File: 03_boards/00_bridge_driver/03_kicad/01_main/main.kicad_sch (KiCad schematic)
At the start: 0 parts

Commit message: Week 0x4 - Spatial ROMs are hard.... (#25)
* Reference document with bootstrap selection calculations

* Boot strap capacitors, resistors and diode work for triple half bridge driver

* Few small changes to reduced order model

* Reduced order model under FOC control

* Finished initial reduced order model

* Custom motor model that needs to be validated and graphs

* Rename to 00_reduced_order_model and Updated readme.md

* Few changes to the model model & Selected Boot Diodes

* Began work on the refactored reduced order model

* New parameter file, removed library and added derived equations

* Initial draft of reduced order model

* Moving pole equation around. Solver not working.

* Issues with the field modelling

* Few additional changes before merge
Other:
- added sheet Drivers (Drivers.kicad_sch)
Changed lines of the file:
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@@
+		)
+	)
+	(sheet
+		(at 238.76 144.78)
+		(size 26.67 3.81)
+		(exclude_from_sim no)
+		(in_bom yes)
+		(on_board yes)
+		(dnp no)
+		(fields_autoplaced yes)
+		(stroke
+			(width 0.1524)
+			(type solid)
+		)
+		(fill
+			(color 0 0 0 0)
+		)
+		(property "Sheetname" "Drivers"
+			(at 238.76 144.0684 0)
+			(show_name no)
+			(do_not_autoplace no)
+			(effects
+				(font
+					(size 1.27 1.27)
+				)
+				(justify left bottom)
+			)
+		)
+		(property "Sheetfile" "Drivers.kicad_sch"
+			(at 238.76 149.1746 0)
+			(show_name no)
+			(do_not_autoplace no)
+			(effects
+				(font
+					(size 1.27 1.27)
+				)
+				(justify left top)
+			)
+		)
+		(instances
+			(project "main"
+				(path "/221b5544-ca14-4503-b001-a85fc346b8a9"
+					(page "3")
+				)
+			)
 		)
 	)

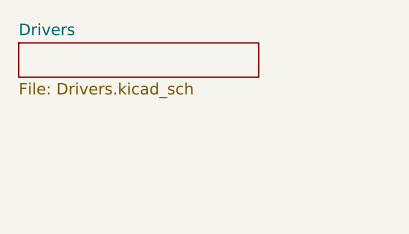
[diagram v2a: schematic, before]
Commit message: Triple bridge driver layout
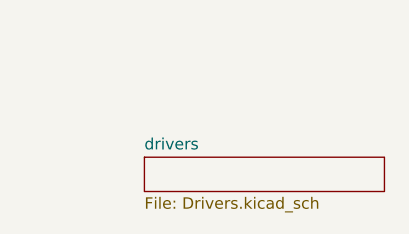
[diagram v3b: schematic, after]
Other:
- sheet Drivers renamed drivers
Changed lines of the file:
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@@
 	)
 	(sheet
-		(at 238.76 144.78)
+		(at 252.73 157.48)
 		(size 26.67 3.81)
 		(exclude_from_sim no)
@@
 			(color 0 0 0 0)
 		)
-		(property "Sheetname" "Drivers"
-			(at 238.76 144.0684 0)
+		(property "Sheetname" "drivers"
+			(at 252.73 156.7684 0)
 			(show_name no)
 			(do_not_autoplace no)
@@
 		)
 		(property "Sheetfile" "Drivers.kicad_sch"
-			(at 238.76 149.1746 0)
+			(at 252.73 161.8746 0)
 			(show_name no)
 			(do_not_autoplace no)

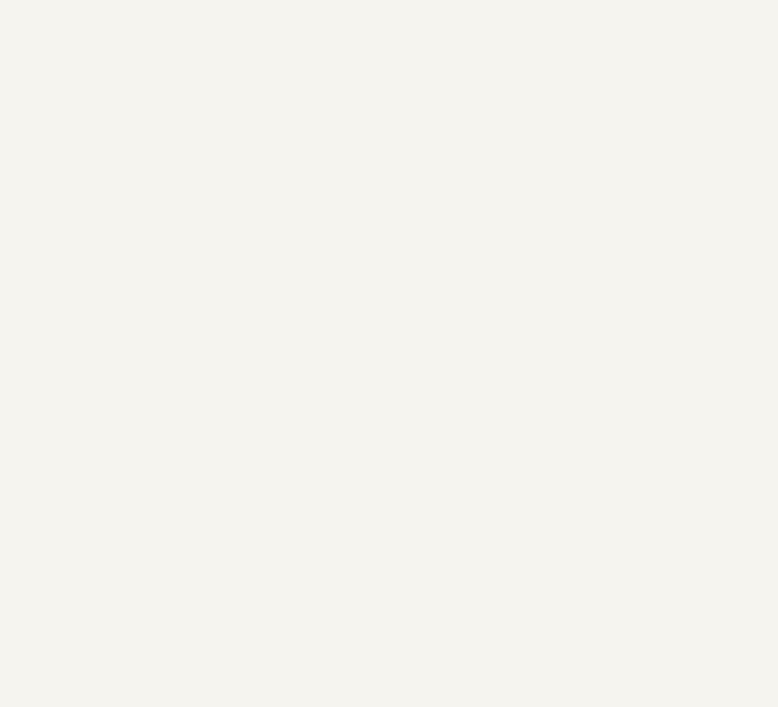
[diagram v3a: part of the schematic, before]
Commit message: Updated the readmes a bit and moved the analytical to 00_analytical
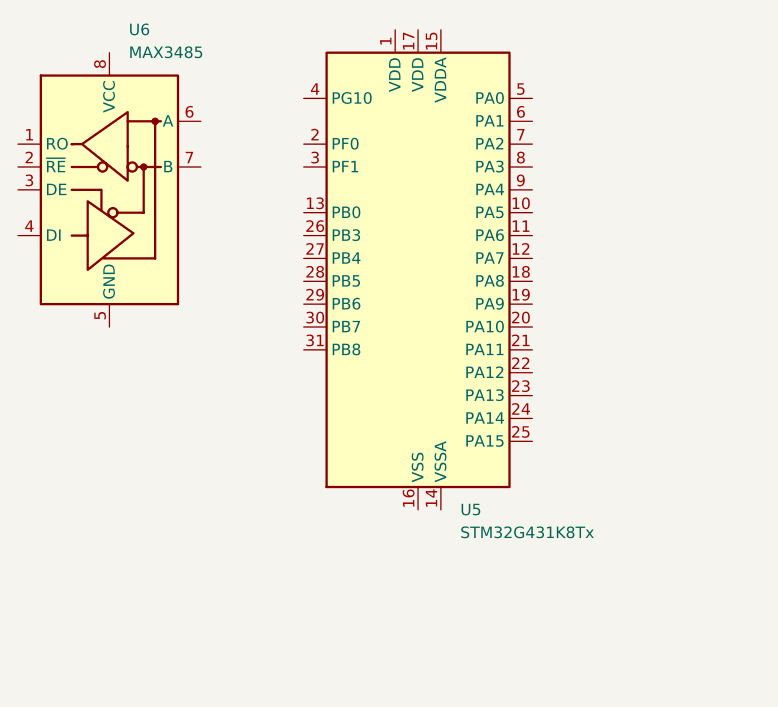
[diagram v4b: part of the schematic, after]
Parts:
- added U5: STM32G431K8Tx, Package_QFP:LQFP-32_7x7mm_P0.8mm, symbol MCU_ST_STM32G4:STM32G431K8Tx
- added U6: MAX3485, Package_SO:SOIC-8_3.9x4.9mm_P1.27mm, symbol Interface_UART:MAX3485
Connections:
- new net: U5.16 (VSS), U5.32 (VSS)
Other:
- title: Triple Bridge Driver -> Bridge Driver
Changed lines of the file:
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@@
 	(paper "A4")
 	(title_block
-		(title "Triple Bridge Driver")
+		(title "Bridge Driver")
 		(date "2026-08-03")
 		(rev "0")
@@
 		)
 	)
+	(symbol
+		(lib_id "Interface_UART:MAX3485")
+		(at 31.75 36.83 0)
+		(unit 1)
+		(body_style 1)
+		(exclude_from_sim no)
+		(in_bom yes)
+		(on_board yes)
+		(in_pos_files yes)
+		(dnp no)
+		(fields_autoplaced yes)
+		(property "Reference" "U6"
+			(at 33.8933 19.05 0)
+			(show_name no)
+			(do_not_autoplace no)
+			(effects
+				(font
+					(size 1.27 1.27)
+				)
+				(justify left)
+			)
+		)
+		(property "Value" "MAX3485"
+			(at 33.8933 21.59 0)
+			(show_name no)
+			(do_not_autoplace no)
+			(effects
+				(font
+					(size 1.27 1.27)
+				)
+				(justify left)
+			)
+		)
+		(property "Footprint" "Package_SO:SOIC-8_3.9x4.9mm_P1.27mm"
+			(at 31.75 59.69 0)
+			(hide yes)
+			(show_name no)
+			(do_not_autoplace no)
+			(effects
+				(font
+					(size 1.27 1.27)
+				)
+			)
+		)
+		(property "Datasheet" "https://datasheets.maximintegrated.com/en/ds/MAX3483-MAX3491.pdf"
+			(at 31.75 35.56 0)
+			(hide yes)
+			(show_name no)
+			(do_not_autoplace no)
+			(effects
+				(font
+					(size 1.27 1.27)
+				)
+			)
+		)
+		(property "Description" "True RS-485/RS-422, 10Mbps, Slew-Rate Limited, with low-power shutdown, with receiver/driver enable, 32 receiver drive capacitity, DIP-8 and SOIC-8"
+			(at 31.75 36.83 0)
+			(hide yes)
+			(show_name no)
+			(do_not_autoplace no)
+			(effects
+				(font
+					(size 1.27 1.27)
+				)
+			)
+		)
+		(pin "1"
+		)
+		(pin "4"
+		)
+		(pin "7"
+		)
+		(pin "2"
+		)
+		(pin "5"
+		)
+		(pin "6"
+		)
+		(pin "8"
+		)
+		(pin "3"
+		)
+		(instances
+			(project "main"
+				(path "/221b5544-ca14-4503-b001-a85fc346b8a9"
+					(reference "U6")
+					(unit 1)
+				)
+			)
+		)
+	)
+	(symbol
+		(lib_id "MCU_ST_STM32G4:STM32G431K8Tx")
+		(at 66.04 46.99 0)
+		(unit 1)
+		(body_style 1)
+		(exclude_from_sim no)
+		(in_bom yes)
+		(on_board yes)
+		(in_pos_files yes)
+		(dnp no)
+		(fields_autoplaced yes)
+		(property "Reference" "U5"
+			(at 70.7233 72.39 0)
+			(show_name no)
+			(do_not_autoplace no)
+			(effects
+				(font
+					(size 1.27 1.27)
+				)
+				(justify left)
+			)
+		)
+		(property "Value" "STM32G431K8Tx"
+			(at 70.7233 74.93 0)
+			(show_name no)
+			(do_not_autoplace no)
+			(effects
+				(font
+					(size 1.27 1.27)
+				)
+				(justify left)
+			)
+		)
+		(property "Footprint" "Package_QFP:LQFP-32_7x7mm_P0.8mm"
+			(at 55.88 69.85 0)
+			(hide yes)
+			(show_name no)
+			(do_not_autoplace no)
+			(effects
+				(font
+					(size 1.27 1.27)
+				)
+				(justify right)
+			)
+		)
+		(property "Datasheet" "https://www.st.com/resource/en/datasheet/stm32g431k8.pdf"
+			(at 66.04 46.99 0)
+			(hide yes)
+			(show_name no)
+			(do_not_autoplace no)
+			(effects
+				(font
+					(size 1.27 1.27)
+				)
+			)
+		)
+		(property "Description" "STMicroelectronics Arm Cortex-M4 MCU, 64KB flash, 32KB RAM, 170 MHz, 1.71-3.6V, 26 GPIO, LQFP32"
+			(at 66.04 46.99 0)
+			(hide yes)
+			(show_name no)
+			(do_not_autoplace no)
+			(effects
+				(font
+					(size 1.27 1.27)
+				)
+			)
+		)
+		(pin "4"
+		)
+		(pin "6"
+		)
+		(pin "11"
+		)
+		(pin "10"
+		)
+		(pin "16"
+		)
+		(pin "15"
+		)
+		(pin "14"
+		)
+		(pin "9"
+		)
+		(pin "23"
+		)
+		(pin "7"
+		)
+		(pin "2"
+		)
+		(pin "1"
+		)
+		(pin "3"
+		)
+		(pin "5"
+		)
+		(pin "8"
+		)
+		(pin "12"
+		)
+		(pin "13"
+		)
+		(pin "17"
+		)
+		(pin "18"
+		)
+		(pin "19"
+		)
+		(pin "20"
+		)
+		(pin "21"
+		)
+		(pin "22"
+		)
+		(pin "29"
+		)
+		(pin "31"
+		)
+		(pin "30"
+		)
+		(pin "28"
+		)
+		(pin "24"
+		)
+		(pin "25"
+		)
+		(pin "27"
+		)
+		(pin "32"
+		)
+		(pin "26"
+		)
+		(instances
+			(project "main"
+				(path "/221b5544-ca14-4503-b001-a85fc346b8a9"
+					(reference "U5")
+					(unit 1)
+				)
+			)
+		)
+	)

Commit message: Continued the driver board
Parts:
- added C12, C13: 30pf, symbol Device:C
- added C14, C15, C17, C21: 100nf, symbol Device:C
- added C16, C19: 10uf, symbol Device:C
- added C18: 1uf, symbol Device:C
- added C20: 22uf, symbol Device:C
- added CAN, J1, STEP: 01x02, symbol Connector_Generic:Conn_01x02
- added D16: LED, symbol Device:LED
- added FB1: BLM18AG601SN1D, symbol Device:FerriteBead
- added INT1: 01x04, symbol Connector_Generic:Conn_01x04
- added R11: 120, symbol Device:R
- added R12, R13: 10, symbol Device:R
- added R14, R15, R18: 220, symbol Device:R
- added R16, R17: 10K, symbol Device:R
- added SW1, SW2: SW_Push, symbol Switch:SW_Push
- added U7: LD1117V33, Package_TO_SOT_THT:TO-220-3_Vertical, symbol Regulator_Linear:LD1117V33
- added Y1: ECS-80-20-18-TR, ECS-80-20-18-TR:XTAL_ECS-80-20-18-TR, symbol ECS-80-20-18-TR:ECS-80-20-18-TR
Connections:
- net RS_RC: now reaches U6.1 (RO)
- net RS_RC: now also U5.27 (PB4), U5.28 (PB5)
- net RS_EN: now reaches U6.2 (~{RE})
- net RS_TOG: now reaches U6.3 (DE)
- net RS_TOG: now also U5.30 (PB7)
- net RS_DRI: now reaches U6.4 (DI)
- net RS_DRI: now also U5.29 (PB6)
- net GND: now reaches U6.5 (GND)
- net GND: now also U5.14 (VSSA), U5.16 (VSS), U5.32 (VSS), C12.2, C13.2, C14.2, C15.2, C16.2, C17.2, C18.2, C19.2, C20.2, C21.2, D16.1 (K), INT1.1 (Pin_1), J1.1 (Pin_1), R17.2, SW2.2, U7.1 (GND)
- net at U6.6 (A): now also R12.2
- net at U6.7 (B): now also R13.2
- net +3.3V: now reaches U6.8 (VCC)
- net +3.3V: now also C16.1, FB1.1, R14.1, U7.2 (VO)
- net VDDA: now reaches U5.1 (VDD)
- net VDDA: now also U5.15 (VDDA), U5.17 (VDD), C17.1, C18.1, C19.1, C20.1, FB1.2, R16.1
- net -STEP: now reaches U5.19 (PA9)
- net -STEP: now also STEP.1 (Pin_1)
- net OSC_OUT: now reaches U5.2 (PF0)
- net OSC_OUT: now also C13.1, Y1.2, Y1.3
- net +STEP: now reaches U5.20 (PA10)
- net +STEP: now also STEP.2 (Pin_2)
- net at U5.22 (PA12): now also R18.1
- net OSC_IN: now reaches U5.3 (PF1)
- net OSC_IN: now also C12.1, Y1.1, Y1.4
- net BOOT: now reaches U5.31 (PB8)
- net BOOT: now also C14.1, R17.1, SW1.2
- net NRST: now reaches U5.4 (PG10)
- net NRST: now also C15.1, R15.1, R16.2
- new net: R14.2, SW1.1
- new net: D16.2 (A), R18.2
- new net: R15.2, SW2.1
- new net +24V: J1.2 (Pin_2)
- new net +5V: C21.1, INT1.4 (Pin_4), U7.3 (VI)
- new net +CAN: CAN.2 (Pin_2)
- new net -CAN: CAN.1 (Pin_1)
- new net D_N: INT1.2 (Pin_2), INT1.3 (Pin_3), R11.2, R13.1
- new net D_P: R11.1, R12.1
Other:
- note added: "8 Mhz Oscillator"
- note added: "Boot / Reset"
- note added: "Controller (170 Mhz)"
- note added: "RS-485/RS-422 Terminations"
- note added: "RS-485/RS-422 Transceiver"
- note added: "VDDA Decoupling"
- moved on the sheet: U5, U6

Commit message: Alot of the schematic finished
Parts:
- added C22, C24: 680uF, symbol Device:C
- added C23, C25: 220uF, symbol Device:C
- added D17, D18: 1N5824, Diode_THT:D_DO-201AD_P15.24mm_Horizontal, symbol Diode:1N5822
- added L1: 33uH, symbol Device:L
- added L2: 68uH, symbol Device:L
- added PH1: 01x03, symbol Connector_Generic:Conn_01x03
- added PRO1: 01x06, symbol Connector_Generic:Conn_01x06
- added U8: LM2596S-5, Package_TO_SOT_SMD:TO-263-5_TabPin3, symbol Regulator_Switching:LM2596S-5
- added U9: LM2596S-12, Package_TO_SOT_SMD:TO-263-5_TabPin3, symbol Regulator_Switching:LM2596S-12
- renumbered CAN to CAN1, STEP to STEP1
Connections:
- net +24V: now also C24.1, U9.1 (VIN)
- net +5V: now also C23.1, L1.2, PRO1.6 (Pin_6), U8.4 (FB)
- net +CAN: now also U5.12 (PA7)
- net +STEP: now also U5.19 (PA9); no longer U5.20 (PA10)
- net -CAN: now also U5.18 (PA8)
- net -STEP: now also U5.20 (PA10); no longer U5.19 (PA9)
- net GND: now also C22.2, C23.2, C24.2, C25.2, D17.2 (A), D18.2 (A), PRO1.4 (Pin_4), U8.3 (GND), U8.5 (~{ON}/OFF), U9.3 (GND), U9.5 (~{ON}/OFF)
- net NRST: now also PRO1.2 (Pin_2)
- net PHB_PWM: now reaches U5.10 (PA5)
- net DRI_ENA: now reaches U5.13 (PB0)
- net PHA_PWM: now reaches U5.21 (PA11)
- net SWDIO: now reaches U5.23 (PA13)
- net SWDIO: now also PRO1.3 (Pin_3)
- net SWCLK: now reaches U5.24 (PA14)
- net SWCLK: now also PRO1.5 (Pin_5)
- net PHC_PWM: now reaches U5.25 (PA15)
- net SWO: now reaches U5.26 (PB3)
- net SWO: now also PRO1.1 (Pin_1)
- net CS1+: now reaches U5.6 (PA1)
- net CS1-: now reaches U5.7 (PA2)
- net CS2+: now reaches U5.8 (PA3)
- net CS2-: now reaches U5.9 (PA4)
- new net: D17.1 (K), L1.1, U8.2 (OUT)
- new net: D18.1 (K), L2.1, U9.2 (OUT)
- new net +12V: C22.1, C25.1, L2.2, U8.1 (VIN), U9.4 (FB)
- new net PA: PH1.3 (Pin_3)
- new net PB: PH1.2 (Pin_2)
- new net PC: PH1.1 (Pin_1)
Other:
- added sheet current (current.kicad_sch)
- note added: "3-Phase Interface"
- note added: "Control Interfaces"
- note added: "Low dropout regulator (5V to 3.3V)"
- note added: "Power & Interconnect"
- note added: "Programming Interface"
- note added: "Step down regulator (12V to 5V)"
- note added: "Step down regulator (24V to 12V)"
- note added: "WARNING: For current sensing, use either the `1 mΩ`, `3 mΩ`, or `10 mΩ` shunt resistor. Do not use more than a single path, or the driver will not function correctly."
- moved on the sheet: C12, C13, C14, C15, C16, C17, C18, C19, C20, C21, CAN1, D16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

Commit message: Draft Schematic Finished
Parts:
- added C26: 0.68uF, symbol Device:C
- added C27: 4.7uF, symbol Device:C
- added L3: 68uH, symbol Device:L
- added L4: 10uH, symbol Device:L
- added U14: CME0512S3C, CME_SC_MUR, symbol 2026-08-29_14-59-18:CME0512S3C
- added U15: CME0303S3C, CME_SC_MUR, symbol 2026-08-29_14-59-18:CME0512S3C
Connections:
- net +12V: now also U15.2 (+VIN)
- net +5V: now also U14.2 (+VIN)
- net GND: now also U14.1 (-VIN), U15.1 (-VIN)
- new net: L4.1, U15.4 (+VOUT)
- new net: L3.1, U14.4 (+VOUT)
- new net +12VIS: C27.1, L4.2
- new net +3.3VIS: C26.1, L3.2
- new net PGND: C26.2, C27.2, U14.3 (-VOUT), U15.3 (-VOUT)
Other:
- note added: "Isolated 12V Supply"

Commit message: Simulation for current sensors and such
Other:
- note added: "F, C"
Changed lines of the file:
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@@
 		(rev "0")
 	)
+	(text "F, C"
+		(exclude_from_sim no)
+		(at 199.898 52.578 0)
+		(effects
+			(font
+				(size 1.27 1.27)
+			)
+		)
+	)
 	(text "3-Phase Interface\n\n\n"
 		(exclude_from_sim no)
@@
 		)
 	)
+	(text "F, C"
+		(exclude_from_sim no)
+		(at 140.97 91.44 0)
+		(effects
+			(font
+				(size 1.27 1.27)
+			)
+		)
+	)
+	(text "F, C"
+		(exclude_from_sim no)
+		(at 153.67 52.07 0)
+		(effects
+			(font
+				(size 1.27 1.27)
+			)
+		)
+	)
 	(text "Power & Interconnect\n"
 		(exclude_from_sim no)
@@
 		)
 	)
+	(text "F, C"
+		(exclude_from_sim no)
+		(at 97.79 158.242 0)
+		(effects
+			(font
+				(size 1.27 1.27)
+			)
+		)
+	)
+	(text "F, C"
+		(exclude_from_sim no)
+		(at 106.68 168.148 0)
+		(effects
+			(font
+				(size 1.27 1.27)
+			)
+		)
+	)
 	(text "Low dropout regulator (5V to 3.3V)\n"
 		(exclude_from_sim no)
@@
 		)
 	)
+	(text "F, C"
+		(exclude_from_sim no)
+		(at 136.144 109.22 0)
+		(effects
+			(font
+				(size 1.27 1.27)
+			)
+		)
+	)
 	(text "VDDA Decoupling\n"
 		(exclude_from_sim no)
@@
 		)
 	)
+	(text "F, C"
+		(exclude_from_sim no)
+		(at 71.882 50.038 0)
+		(effects
+			(font
+				(size 1.27 1.27)
+			)
+		)
+	)
 	(text "Controller (170 Mhz)\n"
 		(exclude_from_sim no)
@@
 		)
 	)
+	(text "F, C"
+		(exclude_from_sim no)
+		(at 62.992 59.69 0)
+		(effects
+			(font
+				(size 1.27 1.27)
+			)
+		)
+	)
+	(text "F, C"
+		(exclude_from_sim no)
+		(at 28.448 58.928 0)
+		(effects
+			(font
+				(size 1.27 1.27)
+			)
+		)
+	)
 	(text "Step down regulator (24V to 12V)\n"
 		(exclude_from_sim no)
@@
 		)
 	)
+	(text "F, C"
+		(exclude_from_sim no)
+		(at 134.112 44.196 0)
+		(effects
+			(font
+				(size 1.27 1.27)
+			)
+		)
+	)
 	(text "Isolated 12V Supply"
 		(exclude_from_sim no)
@@
 		)
 	)
+	(text "F, C"
+		(exclude_from_sim no)
+		(at 30.48 114.554 0)
+		(effects
+			(font
+				(size 1.27 1.27)
+			)
+		)
+	)
 	(text "RS-485/RS-422 Transceiver\n"
 		(exclude_from_sim no)
@@
 		)
 	)
+	(text "F, C"
+		(exclude_from_sim no)
+		(at 199.39 36.322 0)
+		(effects
+			(font
+				(size 1.27 1.27)
+			)
+		)
+	)
 	(text "WARNING:\nFor current sensing, use either the `1 mΩ`, `3 mΩ`, or `10 mΩ` shunt resistor. Do not \nuse more than a single path, or the driver will not function correctly."
 		(exclude_from_sim no)
@@
 		(effects
 			(font
+				(size 1.27 1.27)
+			)
+		)
+	)
+	(text "F, C"
+		(exclude_from_sim no)
+		(at 34.29 156.21 0)
+		(effects
+			(font
+				(size 1.27 1.27)
+			)
+		)
+	)
+	(text "F, C"
+		(exclude_from_sim no)
+		(at 31.496 74.676 0)
+		(effects
+			(font
+				(size 1.27 1.27)
+			)
+		)
+	)
+	(text "F, C"
+		(exclude_from_sim no)
+		(at 73.152 109.728 0)
+		(effects
+			(font
